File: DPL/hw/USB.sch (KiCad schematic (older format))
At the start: 5 parts, among them J7 USB_B_Micro

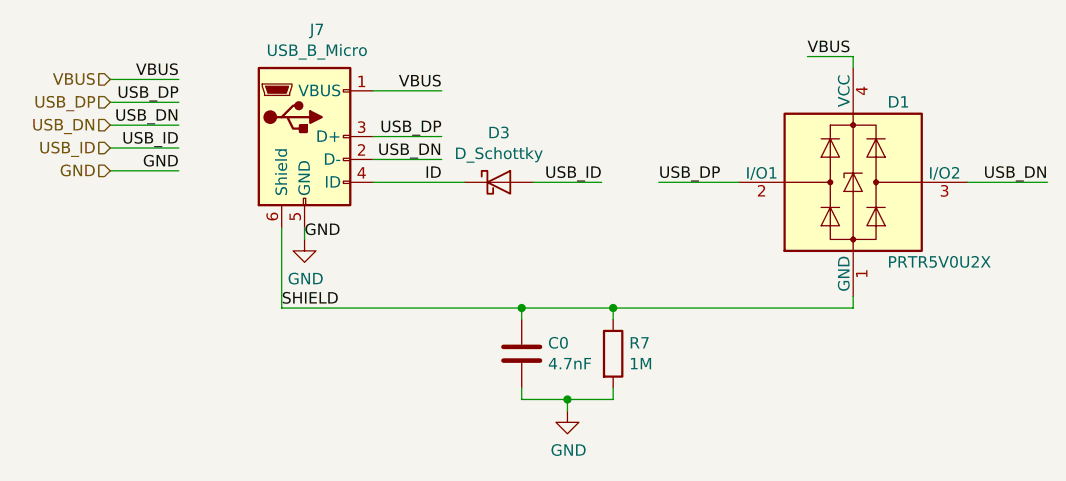
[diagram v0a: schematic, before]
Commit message: Started new design of the DPL payload.
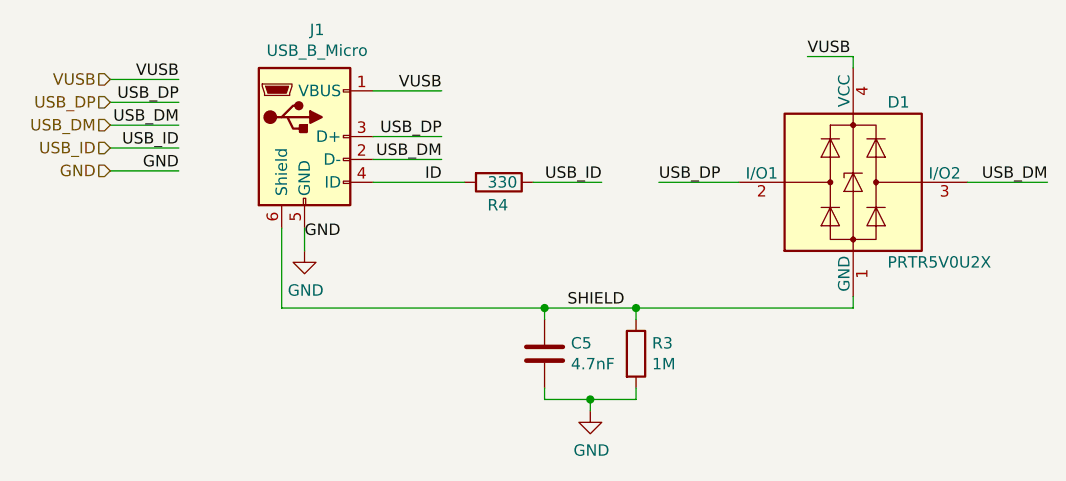
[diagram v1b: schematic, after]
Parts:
- removed D3: D_Schottky, Diode_SMD:D_SOD-523, symbol Device:D_Schottky
- added R4: 330, Resistor_SMD:R_0603_1608Metric_Pad1.05x0.95mm_HandSolder, symbol Device:R
- renumbered C0 to C5, J7 to J1, R7 to R3
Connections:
- net ID: now also R4.2
- net USB_ID: now also R4.1
- net USB_DN renamed USB_DM
- net VBUS renamed VUSB
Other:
- moved on the sheet: C5, R3
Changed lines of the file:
@@
 EESchema Schematic File Version 5
 LIBS:DPL-cache
-EELAYER 29 0
+EELAYER 30 0
 EELAYER END
 $Descr A4 11693 8268
 encoding utf-8
-Sheet 2 3
+Sheet 3 5
 Title ""
 Date ""
@@
 Comment3 ""
 Comment4 ""
+Comment5 ""
+Comment6 ""
+Comment7 ""
+Comment8 ""
+Comment9 ""
 $EndDescr
 $Comp
-L Connector:USB_B_Micro J7
+L Connector:USB_B_Micro J1
 U 1 1 5B62635D
 P 5300 3350
-F 0 "J7" H 5355 3817 50  0000 C CNN
+F 0 "J1" H 5355 3817 50  0000 C CNN
 F 1 "USB_B_Micro" H 5355 3726 50  0000 C CNN
 F 2 "Connector_USB:USB_Micro-B_Molex_47346-0001" H 5450 3300 50  0001 C CNN
@@
 $EndComp
 Text Label 5900 3150 2    50   ~ 0
-VBUS
+VUSB
 Text Label 5900 3350 2    50   ~ 0
 USB_DP
 Text Label 5900 3450 2    50   ~ 0
-USB_DN
+USB_DM
 Text Label 6600 3550 2    50   ~ 0
 USB_ID
+Text Label 5300 3800 0    50   ~ 0
+GND
 $Comp
 L power:GND #PWR0102
 U 1 1 5B62BD38
-P 5300 3800
-F 0 "#PWR0102" H 5300 3550 50  0001 C CNN
-F 1 "GND" H 5305 3627 50  0000 C CNN
-F 2 "" H 5300 3800 50  0001 C CNN
-F 3 "" H 5300 3800 50  0001 C CNN
-	1    5300 3800
+P 5300 3850
+F 0 "#PWR0102" H 5300 3600 50  0001 C CNN
+F 1 "GND" H 5305 3677 50  0000 C CNN
+F 2 "" H 5300 3850 50  0001 C CNN
+F 3 "" H 5300 3850 50  0001 C CNN
+	1    5300 3850
 	1    0    0    -1
 $EndComp
@@
 AR Path="/5B62BD6A" Ref="D1"  Part="1"
 AR Path="/5B626331/5B62BD6A" Ref="D1"  Part="1"
-AR Path="/5CF85FE2/5B62BD6A" Ref="D1"  Part="1"
 F 0 "D1" H 7850 3900 50  0000 L CNN
 F 1 "PRTR5V0U2X" H 7850 3200 50  0000 L CNN
@@
 $EndComp
 $Comp
-L Device:R R7
+L Device:R R3
 U 1 1 5B62BE0D
-P 6650 4300
-F 0 "R7" H 6720 4346 50  0000 L CNN
-F 1 "1M" H 6720 4255 50  0000 L CNN
-F 2 "Resistor_SMD:R_0603_1608Metric_Pad1.05x0.95mm_HandSolder" V 6580 4300 50  0001 C CNN
-F 3 "~" H 6650 4300 50  0001 C CNN
-	1    6650 4300
+P 6750 4300
+F 0 "R3" H 6820 4346 50  0000 L CNN
+F 1 "1M" H 6820 4255 50  0000 L CNN
+F 2 "Resistor_SMD:R_0603_1608Metric_Pad1.05x0.95mm_HandSolder" V 6680 4300 50  0001 C CNN
+F 3 "~" H 6750 4300 50  0001 C CNN
+	1    6750 4300
 	1    0    0    -1
 $EndComp
 $Comp
-L Device:C C0
+L Device:C C5
 U 1 1 5B62BE71
-P 6250 4300
-F 0 "C0" H 6365 4346 50  0000 L CNN
-F 1 "4.7nF" H 6365 4255 50  0000 L CNN
-F 2 "Capacitor_SMD:C_0603_1608Metric_Pad1.05x0.95mm_HandSolder" H 6288 4150 50  0001 C CNN
-F 3 "~" H 6250 4300 50  0001 C CNN
-	1    6250 4300
+P 6350 4300
+F 0 "C5" H 6465 4346 50  0000 L CNN
+F 1 "4.7nF" H 6465 4255 50  0000 L CNN
+F 2 "Capacitor_SMD:C_0603_1608Metric_Pad1.05x0.95mm_HandSolder" H 6388 4150 50  0001 C CNN
+F 3 "~" H 6350 4300 50  0001 C CNN
+	1    6350 4300
 	1    0    0    -1
 $EndComp
 Wire Wire Line
-	6250 4150 6250 4100
+	6350 4150 6350 4100
 Wire Wire Line
-	6650 4100 6650 4150
+	6750 4100 6750 4150
 Wire Wire Line
-	7700 4050 7700 4100
+	6350 4450 6350 4500
 Wire Wire Line
-	6250 4450 6250 4500
+	6350 4500 6550 4500
 Wire Wire Line
-	6250 4500 6450 4500
+	6750 4500 6750 4450
 Wire Wire Line
-	6650 4500 6650 4450
+	6550 4500 6550 4550
+Connection ~ 6550 4500
 Wire Wire Line
-	6450 4500 6450 4550
-Connection ~ 6450 4500
-Wire Wire Line
-	6450 4500 6650 4500
+	6550 4500 6750 4500
 $Comp
 L power:GND #PWR0103
 U 1 1 5BA44753
-P 6450 4550
-F 0 "#PWR0103" H 6450 4300 50  0001 C CNN
-F 1 "GND" H 6455 4377 50  0000 C CNN
-F 2 "" H 6450 4550 50  0001 C CNN
-F 3 "" H 6450 4550 50  0001 C CNN
-	1    6450 4550
+P 6550 4550
+F 0 "#PWR0103" H 6550 4300 50  0001 C CNN
+F 1 "GND" H 6555 4377 50  0000 C CNN
+F 2 "" H 6550 4550 50  0001 C CNN
+F 3 "" H 6550 4550 50  0001 C CNN
+	1    6550 4550
 	1    0    0    -1
 $EndComp
@@
 	7700 3000 7500 3000
 Text Label 7500 3000 0    50   ~ 0
-VBUS
+VUSB
 Wire Wire Line
 	7200 3550 6850 3550
@@
 	8200 3550 8550 3550
 Text Label 8550 3550 2    50   ~ 0
-USB_DN
+USB_DM
 Wire Wire Line
 	5600 3350 5900 3350
@@
 	5600 3150 5900 3150
 Text HLabel 4450 3100 0    50   Input ~ 0
-VBUS
+VUSB
 Text HLabel 4450 3200 0    50   Input ~ 0
 USB_DP
 Text HLabel 4450 3300 0    50   Input ~ 0
-USB_DN
+USB_DM
 Text HLabel 4450 3400 0    50   Input ~ 0
 USB_ID
@@
 	4450 3100 4750 3100
 Text Label 4750 3100 2    50   ~ 0
-VBUS
+VUSB
 Text Label 4750 3200 2    50   ~ 0
 USB_DP
 Text Label 4750 3300 2    50   ~ 0
-USB_DN
+USB_DM
 Text Label 4750 3400 2    50   ~ 0
 USB_ID
@@
 Text Label 5900 3550 2    50   ~ 0
 ID
-$Comp
-L Device:D_Schottky D3
-U 1 1 5BB753F5
-P 6150 3550
-F 0 "D3" H 6150 3766 50  0000 C CNN
-F 1 "D_Schottky" H 6150 3675 50  0000 C CNN
-F 2 "Diode_SMD:D_SOD-523" H 6150 3550 50  0001 C CNN
-F 3 "~" H 6150 3550 50  0001 C CNN
-	1    6150 3550
-	1    0    0    -1
-$EndComp
 Wire Wire Line
 	5600 3550 6000 3550
 Wire Wire Line
-	6250 4100 6650 4100
+	6350 4100 6750 4100
 Wire Wire Line
-	7700 4100 6650 4100
-Connection ~ 6650 4100
+	6750 4100 7700 4100
+Connection ~ 6750 4100
 Wire Wire Line
-	6250 4100 5200 4100
+	6350 4100 5200 4100
+Connection ~ 6350 4100
 Wire Wire Line
 	5200 3750 5200 4100
-Connection ~ 6250 4100
 Wire Wire Line
-	5300 3750 5300 3800
-Text Label 5200 4100 0    50   ~ 0
+	5300 3750 5300 3850
+Wire Wire Line
+	7700 4100 7700 4050
+Text Label 6450 4100 0    50   ~ 0
 SHIELD
-Text Label 5300 3800 0    50   ~ 0
-GND
+$Comp
+L Device:R R4
+U 1 1 5D1D507C
+P 6150 3550
+F 0 "R4" V 6250 3500 50  0000 L CNN
+F 1 "330" V 6150 3500 50  0000 L CNN
+F 2 "Resistor_SMD:R_0603_1608Metric_Pad1.05x0.95mm_HandSolder" V 6080 3550 50  0001 C CNN
+F 3 "~" H 6150 3550 50  0001 C CNN
+	1    6150 3550
+	0    1    1    0
+$EndComp
 $EndSCHEMATC
